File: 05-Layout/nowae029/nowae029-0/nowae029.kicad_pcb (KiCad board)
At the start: 2 copper layers, 100 x 99.9 mm, 1 part

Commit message: WiP on microcontroller
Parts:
- added U1: STM32L073CBT6, LQFP:LQFP48_7x7_0.5, F.Cu at (100.0, 108.0)

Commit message: WiP: PCB components placing
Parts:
- added C201: 100n, CAPACITOR:CAPACITOR-0603, F.Cu at (108.6, 107.0)
- added C202: 15p, CAPACITOR:CAPACITOR-0603, F.Cu at (238.7, 79.1)
- added C203: 15p, CAPACITOR:CAPACITOR-0603, F.Cu at (242.0, 79.1)
- added C204: 10u, CAPACITOR:CAPACITOR-1206, F.Cu at (107.2, 108.6)
- added C205: 100n, CAPACITOR:CAPACITOR-0603, F.Cu at (251.8, 72.2)
- added C206: 10u, CAPACITOR:CAPACITOR-1206, F.Cu at (236.6, 72.7)
- added C207: 10u, CAPACITOR:CAPACITOR-1206, F.Cu at (242.0, 69.2)
- added C208: 100n, CAPACITOR:CAPACITOR-0603, F.Cu at (245.2, 79.1)
- added C209: 10u, CAPACITOR:CAPACITOR-1206, F.Cu at (236.6, 76.1)
- added C210: 100n, CAPACITOR:CAPACITOR-0603, F.Cu at (251.8, 74.6)
- added C211: 100n, CAPACITOR:CAPACITOR-0603, F.Cu at (255.1, 72.2)
- added C301: 100n, CAPACITOR:CAPACITOR-0603, F.Cu at (165.1, 103.6)
- added C302: 100n, CAPACITOR:CAPACITOR-0603, F.Cu at (168.4, 103.6)
- added C303: 100n, CAPACITOR:CAPACITOR-0603, F.Cu at (171.6, 103.6)
- added C401: 1u, CAPACITOR:CAPACITOR-1206, F.Cu at (274.3, 69.2)
- added C402: 1u, CAPACITOR:CAPACITOR-1206, F.Cu at (268.8, 72.7)
- added C501: 4u7, CAPACITOR:CAPACITOR-1206, F.Cu at (91.6, 140.8)
- added C502: 100n, CAPACITOR:CAPACITOR-0603, F.Cu at (105.8, 145.0)
- added C503: 100n, CAPACITOR:CAPACITOR-0603, F.Cu at (114.6, 145.6)
- added C504: 100n, CAPACITOR:CAPACITOR-0603, F.Cu at (116.2, 145.6)
- added C601: 100n, CAPACITOR:CAPACITOR-0603, F.Cu at (165.1, 144.5)
- added C602: 100n, CAPACITOR:CAPACITOR-0603, F.Cu at (168.4, 144.5)
- added C603: 100n, CAPACITOR:CAPACITOR-0603, F.Cu at (171.6, 144.5)
- added D401: MBR0520, DIODE:DIODE-SOD123, F.Cu at (262.6, 72.1)
- added D402: MBR0520, DIODE:DIODE-SOD123, F.Cu at (262.6, 69.0)
- added D501: ESDA25P35, DIODE:DIODE-0805, F.Cu at (86.5, 141.0)
- added DL301: MISC, LEDs:LED-1206, F.Cu at (104.7, 76.1)
- added DL302: MISC, LEDs:LED-1206, B.Cu at (104.8, 76.0)
- added DL303: MISC, LEDs:LED-1206, F.Cu at (109.8, 79.0)
- added DL304: MISC, LEDs:LED-1206, F.Cu at (189.2, 69.2)
- added DL305: MISC, LEDs:LED-1206, F.Cu at (104.7, 91.1)
- added DL306: MISC, LEDs:LED-1206, F.Cu at (178.3, 83.2)
- added DL307: MISC, LEDs:LED-1206, F.Cu at (109.8, 94.0)
- added DL308: MISC, LEDs:LED-1206, F.Cu at (180.7, 79.8)
- added DL309: MISC, LEDs:LED-1206, F.Cu at (115.0, 97.0)
- added DL310: MISC, LEDs:LED-1206, F.Cu at (172.3, 90.3)
- added DL311: MISC, LEDs:LED-1206, F.Cu at (120.4, 100.0)
- added DL312: MISC, LEDs:LED-1206, F.Cu at (195.2, 69.2)
- added DL313: MISC, LEDs:LED-1206, F.Cu at (114.7, 111.7)
- added DL314: MISC, LEDs:LED-1206, F.Cu at (178.3, 86.7)
- added DL315: MISC, LEDs:LED-1206, F.Cu at (120.2, 114.6)
- added DL316: MISC, LEDs:LED-1206, F.Cu at (166.2, 100.7)
- added DL317: MISC, LEDs:LED-1206, F.Cu at (125.4, 117.6)
- added DL318: MISC, LEDs:LED-1206, F.Cu at (186.8, 79.6)
- added DL319: MISC, LEDs:LED-1206, F.Cu at (130.6, 120.6)
- added DL320: MISC, LEDs:LED-1206, F.Cu at (178.3, 90.1)
- added DL321: MISC, LEDs:LED-1206, F.Cu at (105.1, 121.1)
- added DL322: MISC, LEDs:LED-1206, F.Cu at (201.3, 69.2)
- added DL323: MISC, LEDs:LED-1206, F.Cu at (112.0, 124.8)
- added DL324: MISC, LEDs:LED-1206, F.Cu at (184.4, 86.7)
- added DL325: MISC, LEDs:LED-1206, F.Cu at (118.9, 128.9)
- added DL326: MISC, LEDs:LED-1206, F.Cu at (172.3, 100.7)
- added DL327: MISC, LEDs:LED-1206, F.Cu at (125.5, 132.5)
- added DL328: MISC, LEDs:LED-1206, F.Cu at (192.8, 79.6)
- added DL329: MISC, LEDs:LED-1206, F.Cu at (132.4, 136.4)
- added DL330: MISC, LEDs:LED-1206, F.Cu at (184.4, 90.1)
- added DL331: MISC, LEDs:LED-1206, F.Cu at (139.4, 140.4)
- added DL332: MISC, LEDs:LED-1206, F.Cu at (207.3, 69.2)
- added DL333: MISC, LEDs:LED-1206, F.Cu at (178.3, 97.0)
- added DL334: MISC, LEDs:LED-1206, F.Cu at (190.4, 86.5)
- added DL335: MISC, LEDs:LED-1206, F.Cu at (196.5, 83.0)
- added DL336: MISC, LEDs:LED-1206, F.Cu at (178.3, 100.5)
- added DL337: MISC, LEDs:LED-1206, F.Cu at (184.4, 93.6)
- added DL338: MISC, LEDs:LED-1206, F.Cu at (198.9, 79.6)
- added DL339: MISC, LEDs:LED-1206, F.Cu at (204.9, 76.1)
- added DL340: MISC, LEDs:LED-1206, F.Cu at (190.4, 89.9)
- added DL341: MISC, LEDs:LED-1206, F.Cu at (183.1, 69.2)
- added DL342: MISC, LEDs:LED-1206, F.Cu at (213.4, 69.2)
- added DL343: MISC, LEDs:LED-1206, F.Cu at (166.2, 83.4)
- added DL344: MISC, LEDs:LED-1206, F.Cu at (207.3, 72.7)
- added DL345: MISC, LEDs:LED-1206, F.Cu at (174.7, 76.3)
- added DL346: MISC, LEDs:LED-1206, F.Cu at (174.7, 79.8)
- added DL347: MISC, LEDs:LED-1206, F.Cu at (172.3, 83.4)
- added DL348: MISC, LEDs:LED-1206, F.Cu at (166.2, 86.9)
- added DL601: MISC, LEDs:LED-1206, F.Cu at (95.2, 76.0)
- added DL602: MISC, LEDs:LED-1206, F.Cu at (207.3, 113.6)
- added DL603: MISC, LEDs:LED-1206, F.Cu at (90.2, 79.0)
- added DL604: MISC, LEDs:LED-1206, F.Cu at (178.3, 141.4)
- added DL605: MISC, LEDs:LED-1206, F.Cu at (95.0, 91.2)
- added DL606: MISC, LEDs:LED-1206, F.Cu at (190.4, 127.4)
- added DL607: MISC, LEDs:LED-1206, F.Cu at (90.0, 94.0)
- added DL608: MISC, LEDs:LED-1206, F.Cu at (207.3, 110.1)
- added DL609: MISC, LEDs:LED-1206, F.Cu at (84.8, 97.0)
- added DL610: MISC, LEDs:LED-1206, F.Cu at (184.4, 131.0)
- added DL611: MISC, LEDs:LED-1206, F.Cu at (79.4, 100.0)
- added DL612: MISC, LEDs:LED-1206, F.Cu at (192.8, 120.5)
- added DL613: MISC, LEDs:LED-1206, F.Cu at (86.5, 110.9)
- added DL614: MISC, LEDs:LED-1206, F.Cu at (172.3, 141.6)
- added DL615: MISC, LEDs:LED-1206, F.Cu at (80.7, 114.1)
- added DL616: MISC, LEDs:LED-1206, F.Cu at (184.4, 127.6)
- added DL617: MISC, LEDs:LED-1206, F.Cu at (75.0, 117.2)
- added DL618: MISC, LEDs:LED-1206, F.Cu at (201.3, 110.1)
- added DL619: MISC, LEDs:LED-1206, F.Cu at (69.4, 120.4)
- added DL620: MISC, LEDs:LED-1206, F.Cu at (178.3, 131.0)
- added DL621: MISC, LEDs:LED-1206, F.Cu at (94.6, 121.2)
- added DL622: MISC, LEDs:LED-1206, F.Cu at (186.8, 120.5)
- added DL623: MISC, LEDs:LED-1206, F.Cu at (88.2, 124.8)
- added DL624: MISC, LEDs:LED-1206, F.Cu at (166.2, 141.6)
- added DL625: MISC, LEDs:LED-1206, F.Cu at (81.0, 128.8)
- added DL626: MISC, LEDs:LED-1206, F.Cu at (178.3, 127.6)
- added DL627: MISC, LEDs:LED-1206, F.Cu at (74.6, 132.4)
- added DL628: MISC, LEDs:LED-1206, F.Cu at (195.2, 110.1)
- added DL629: MISC, LEDs:LED-1206, F.Cu at (67.6, 136.4)
- added DL630: MISC, LEDs:LED-1206, F.Cu at (172.3, 131.2)
- added DL631: MISC, LEDs:LED-1206, F.Cu at (60.4, 140.4)
- added DL632: MISC, LEDs:LED-1206, F.Cu at (180.7, 120.7)
- added DL633: MISC, LEDs:LED-1206, F.Cu at (166.2, 134.7)
- added DL634: MISC, LEDs:LED-1206, F.Cu at (178.3, 124.1)
- added DL635: MISC, LEDs:LED-1206, F.Cu at (172.3, 127.8)
- added DL636: MISC, LEDs:LED-1206, F.Cu at (189.2, 110.1)
- added DL637: MISC, LEDs:LED-1206, F.Cu at (183.1, 113.6)
- added DL638: MISC, LEDs:LED-1206, F.Cu at (166.2, 131.2)
- added DL639: MISC, LEDs:LED-1206, F.Cu at (180.7, 117.2)
- added DL640: MISC, LEDs:LED-1206, F.Cu at (174.7, 120.7)
- added DL641: MISC, LEDs:LED-1206, F.Cu at (172.3, 124.3)
- added DL642: MISC, LEDs:LED-1206, F.Cu at (166.2, 127.8)
- added DL643: MISC, LEDs:LED-1206, F.Cu at (183.1, 110.1)
- added DL644: MISC, LEDs:LED-1206, F.Cu at (174.7, 117.2)
- added DL645: MISC, LEDs:LED-1206, F.Cu at (166.2, 124.3)
- added DL646: MISC, LEDs:LED-1206, F.Cu at (204.9, 117.0)
- added DL647: MISC, LEDs:LED-1206, F.Cu at (198.9, 120.5)
- added DL648: MISC, LEDs:LED-1206, F.Cu at (213.4, 110.1)
- added P501: 632722110112, CONNECTOR:USB3.1-C_WE-632722110112, F.Cu at (89.6, 145.2)
- added R201: 4k7, RESISTOR:RESISTOR-1206, F.Cu at (247.5, 76.1)
- added R202: 4k7, RESISTOR:RESISTOR-1206, F.Cu at (252.9, 69.2)
- added R203: 4k7, RESISTOR:RESISTOR-1206, F.Cu at (247.5, 72.7)
- added R204: 4k7, RESISTOR:RESISTOR-1206, F.Cu at (242.0, 76.1)
- added R205: 0, RESISTOR:RESISTOR-1206, F.Cu at (247.5, 69.2)
- added R206: 10k, RESISTOR:RESISTOR-1206, F.Cu at (242.0, 72.7)
- added R301: 270, RESISTOR:RESISTOR-1206, F.Cu at (202.5, 83.0)
- added R302: 270, RESISTOR:RESISTOR-1206, F.Cu at (184.4, 97.0)
- added R303: 270, RESISTOR:RESISTOR-1206, F.Cu at (211.0, 76.1)
- added R304: 270, RESISTOR:RESISTOR-1206, F.Cu at (196.5, 89.9)
- added R305: 270, RESISTOR:RESISTOR-1206, F.Cu at (196.5, 86.5)
- added R306: 270, RESISTOR:RESISTOR-1206, F.Cu at (189.8, 97.0)
- added R307: 270, RESISTOR:RESISTOR-1206, F.Cu at (213.4, 72.7)
- added R308: 270, RESISTOR:RESISTOR-1206, F.Cu at (184.4, 100.5)
- added R309: 270, RESISTOR:RESISTOR-1206, F.Cu at (190.4, 93.4)
- added R310: 270, RESISTOR:RESISTOR-1206, F.Cu at (204.9, 79.6)
- added R311: 270, RESISTOR:RESISTOR-1206, F.Cu at (217.7, 93.4)
- added R312: 270, RESISTOR:RESISTOR-1206, F.Cu at (211.6, 100.3)
- added R313: 270, RESISTOR:RESISTOR-1206, F.Cu at (223.7, 86.5)
- added R314: 270, RESISTOR:RESISTOR-1206, F.Cu at (211.6, 96.8)
- added R315: 270, RESISTOR:RESISTOR-1206, F.Cu at (218.3, 89.9)
- added R316: 270, RESISTOR:RESISTOR-1206, F.Cu at (226.7, 79.6)
- added R317: 270, RESISTOR:RESISTOR-1206, F.Cu at (212.2, 93.4)
- added R318: 270, RESISTOR:RESISTOR-1206, F.Cu at (206.2, 100.3)
- added R319: 270, RESISTOR:RESISTOR-1206, F.Cu at (224.3, 83.0)
- added R320: 270, RESISTOR:RESISTOR-1206, F.Cu at (218.3, 86.5)
- added R321: 270, RESISTOR:RESISTOR-1206, F.Cu at (206.2, 96.8)
- added R322: 270, RESISTOR:RESISTOR-1206, F.Cu at (212.8, 89.9)
- added R323: 270, RESISTOR:RESISTOR-1206, F.Cu at (227.3, 76.1)
- added R324: 270, RESISTOR:RESISTOR-1206, F.Cu at (221.3, 79.6)
- added R325: 270, RESISTOR:RESISTOR-1206, F.Cu at (206.8, 93.4)
- added R326: 270, RESISTOR:RESISTOR-1206, F.Cu at (200.7, 100.3)
- added R327: 270, RESISTOR:RESISTOR-1206, F.Cu at (218.9, 83.0)
- added R328: 270, RESISTOR:RESISTOR-1206, F.Cu at (212.8, 86.5)
- added R329: 270, RESISTOR:RESISTOR-1206, F.Cu at (200.7, 96.8)
- added R330: 270, RESISTOR:RESISTOR-1206, F.Cu at (224.3, 72.7)
- added R331: 270, RESISTOR:RESISTOR-1206, F.Cu at (207.4, 89.9)
- added R332: 270, RESISTOR:RESISTOR-1206, F.Cu at (221.9, 76.1)
- added R333: 270, RESISTOR:RESISTOR-1206, F.Cu at (215.8, 79.6)
- added R334: 270, RESISTOR:RESISTOR-1206, F.Cu at (201.3, 93.4)
- added R335: 270, RESISTOR:RESISTOR-1206, F.Cu at (195.3, 100.3)
- added R336: 270, RESISTOR:RESISTOR-1206, F.Cu at (213.4, 83.0)
- added R337: 270, RESISTOR:RESISTOR-1206, F.Cu at (207.4, 86.5)
- added R338: 270, RESISTOR:RESISTOR-1206, F.Cu at (224.9, 69.2)
- added R339: 270, RESISTOR:RESISTOR-1206, F.Cu at (195.3, 96.8)
- added R340: 270, RESISTOR:RESISTOR-1206, F.Cu at (218.8, 72.7)
- added R341: 270, RESISTOR:RESISTOR-1206, F.Cu at (201.9, 89.9)
- added R342: 270, RESISTOR:RESISTOR-1206, F.Cu at (216.4, 76.1)
- added R343: 270, RESISTOR:RESISTOR-1206, F.Cu at (210.4, 79.6)
- added R344: 270, RESISTOR:RESISTOR-1206, F.Cu at (195.9, 93.4)
- added R345: 270, RESISTOR:RESISTOR-1206, F.Cu at (189.8, 100.5)
- added R346: 270, RESISTOR:RESISTOR-1206, F.Cu at (208.0, 83.0)
- added R347: 270, RESISTOR:RESISTOR-1206, F.Cu at (201.9, 86.5)
- added R348: 270, RESISTOR:RESISTOR-1206, F.Cu at (219.4, 69.2)
- added R401: 100k, RESISTOR:RESISTOR-1206, F.Cu at (268.8, 69.2)
- added R402: 100k, RESISTOR:RESISTOR-1206, F.Cu at (262.5, 75.3)
- added R601: 270, RESISTOR:RESISTOR-1206, F.Cu at (95.4, 79.2)
- added R602: 270, RESISTOR:RESISTOR-1206, F.Cu at (217.7, 134.3)
- added R603: 270, RESISTOR:RESISTOR-1206, F.Cu at (91.2, 81.6)
- added R604: 270, RESISTOR:RESISTOR-1206, F.Cu at (218.3, 130.8)
- added R605: 270, RESISTOR:RESISTOR-1206, F.Cu at (184.4, 137.9)
- added R606: 270, RESISTOR:RESISTOR-1206, F.Cu at (223.7, 127.4)
- added R607: 270, RESISTOR:RESISTOR-1206, F.Cu at (196.5, 127.4)
- added R608: 270, RESISTOR:RESISTOR-1206, F.Cu at (202.5, 123.9)
- added R609: 270, RESISTOR:RESISTOR-1206, F.Cu at (184.4, 141.4)
- added R610: 270, RESISTOR:RESISTOR-1206, F.Cu at (190.4, 134.3)
- added R611: 270, RESISTOR:RESISTOR-1206, F.Cu at (204.9, 120.5)
- added R612: 270, RESISTOR:RESISTOR-1206, F.Cu at (211.0, 117.0)
- added R613: 270, RESISTOR:RESISTOR-1206, F.Cu at (196.5, 130.8)
- added R614: 270, RESISTOR:RESISTOR-1206, F.Cu at (189.8, 137.9)
- added R615: 270, RESISTOR:RESISTOR-1206, F.Cu at (213.4, 113.6)
- added R616: 270, RESISTOR:RESISTOR-1206, F.Cu at (219.4, 110.1)
- added R617: 270, RESISTOR:RESISTOR-1206, F.Cu at (201.9, 127.4)
- added R618: 270, RESISTOR:RESISTOR-1206, F.Cu at (208.0, 123.9)
- added R619: 270, RESISTOR:RESISTOR-1206, F.Cu at (189.8, 141.4)
- added R620: 270, RESISTOR:RESISTOR-1206, F.Cu at (195.9, 134.3)
- added R621: 270, RESISTOR:RESISTOR-1206, F.Cu at (210.4, 120.5)
- added R622: 270, RESISTOR:RESISTOR-1206, F.Cu at (216.4, 117.0)
- added R623: 270, RESISTOR:RESISTOR-1206, F.Cu at (201.9, 130.8)
- added R624: 270, RESISTOR:RESISTOR-1206, F.Cu at (218.8, 113.6)
- added R625: 270, RESISTOR:RESISTOR-1206, F.Cu at (195.3, 137.7)
- added R626: 270, RESISTOR:RESISTOR-1206, F.Cu at (224.9, 110.1)
- added R627: 270, RESISTOR:RESISTOR-1206, F.Cu at (207.4, 127.4)
- added R628: 270, RESISTOR:RESISTOR-1206, F.Cu at (213.4, 123.9)
- added R629: 270, RESISTOR:RESISTOR-1206, F.Cu at (195.3, 141.2)
- added R630: 270, RESISTOR:RESISTOR-1206, F.Cu at (201.3, 134.3)
- added R631: 270, RESISTOR:RESISTOR-1206, F.Cu at (215.8, 120.5)
- added R632: 270, RESISTOR:RESISTOR-1206, F.Cu at (221.9, 117.0)
- added R633: 270, RESISTOR:RESISTOR-1206, F.Cu at (207.4, 130.8)
- added R634: 270, RESISTOR:RESISTOR-1206, F.Cu at (224.3, 113.6)
- added R635: 270, RESISTOR:RESISTOR-1206, F.Cu at (200.7, 137.7)
- added R636: 270, RESISTOR:RESISTOR-1206, F.Cu at (212.8, 127.4)
- added R637: 270, RESISTOR:RESISTOR-1206, F.Cu at (218.9, 123.9)
- added R638: 270, RESISTOR:RESISTOR-1206, F.Cu at (200.7, 141.2)
- added R639: 270, RESISTOR:RESISTOR-1206, F.Cu at (206.8, 134.3)
- added R640: 270, RESISTOR:RESISTOR-1206, F.Cu at (221.3, 120.5)
- added R641: 270, RESISTOR:RESISTOR-1206, F.Cu at (227.3, 117.0)
- added R642: 270, RESISTOR:RESISTOR-1206, F.Cu at (212.8, 130.8)
- added R643: 270, RESISTOR:RESISTOR-1206, F.Cu at (206.2, 137.7)
- added R644: 270, RESISTOR:RESISTOR-1206, F.Cu at (218.3, 127.4)
- added R645: 270, RESISTOR:RESISTOR-1206, F.Cu at (224.3, 123.9)
- added R646: 270, RESISTOR:RESISTOR-1206, F.Cu at (206.2, 141.2)
- added R647: 270, RESISTOR:RESISTOR-1206, F.Cu at (212.2, 134.3)
- added R648: 270, RESISTOR:RESISTOR-1206, F.Cu at (226.7, 120.5)
- added U301: TCA9554PWR, SOP:TSSOP16_4.4x5.0_0.65, F.Cu at (110.2, 137.2)
- added U302: TCA9554PWR, SOP:TSSOP16_4.4x5.0_0.65, F.Cu at (124.4, 143.6)
- added U303: TCA9554PWR, SOP:TSSOP16_4.4x5.0_0.65, F.Cu at (176.2, 71.2)
- added U401: TLV70233DBV, SOT:SOT23-5, F.Cu at (273.9, 73.1)
- added U501: FT230XS, SOP:SSOP16_3.9x4.9_0.635, F.Cu at (110.2, 145.2)
- added U601: TCA9554PWR, SOP:TSSOP16_4.4x5.0_0.65, F.Cu at (89.6, 133.8)
- added U602: TCA9554PWR, SOP:TSSOP16_4.4x5.0_0.65, F.Cu at (76.0, 143.6)
- added U603: TCA9554PWR, SOP:TSSOP16_4.4x5.0_0.65, F.Cu at (167.7, 112.1)
- moved G*** 58.3 mm to (180.0, 153.0)
- moved U1 4.03 mm to (100.0, 104.0)
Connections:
- net Net-(U1-Pad15) renamed /Microcontroller/STAR
- net Net-(U1-Pad34) renamed /Microcontroller/SWDIO
- net Net-(U1-Pad37) renamed /Microcontroller/SWCLK
- U1 pad 10: Net-(U1-Pad10) -> /Power Supply/BATTERY_STATUS
- U1 pad 21: Net-(U1-Pad21) -> /B_EXT_SDA
- U1 pad 22: Net-(U1-Pad22) -> /B_EXT_SCL
- U1 pad 23: Net-(U1-Pad23) -> GND
- U1 pad 24: Net-(U1-Pad24) -> /Microcontroller/VDD_MCU
- U1 pad 30: Net-(U1-Pad30) -> /Communication/COMM_RX
- U1 pad 31: Net-(U1-Pad31) -> /Communication/COMM_TX
- U1 pad 35: Net-(U1-Pad35) -> GND
- U1 pad 36: Net-(U1-Pad36) -> /Microcontroller/VDD_MCU
- U1 pad 42: Net-(U1-Pad42) -> /Branch1/BRANCH1_SCL
- U1 pad 43: Net-(U1-Pad43) -> /Branch1/BRANCH1_SDA
- U1 pad 47: Net-(U1-Pad47) -> GND
- U1 pad 48: Net-(U1-Pad48) -> /Microcontroller/VDD_MCU
- U1 pad 7: Net-(U1-Pad7) -> /Microcontroller/RESET
- U1 pad 8: Net-(U1-Pad8) -> GND
- U1 pad 9: Net-(U1-Pad9) -> /Microcontroller/VDD_MCU

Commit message: WiP: components placing
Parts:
- removed U1: STM32L073CBT6, LQFP:LQFP48_7x7_0.5
- added U201: STM32L073CBT6, LQFP:LQFP48_7x7_0.5, F.Cu at (100.0, 105.3)
- DL602, DL604, DL606, DL608, DL610, DL612, DL614, DL616, DL618, DL620, DL622, DL624, DL626, DL628, DL630, DL632, R602, R604, R606, R608, R610, R612, R614, R616, R618, R620, R622, R624, R626, R628, R630, R632: moved to B.Cu
- moved R201 173.7 mm to (92.0, 153.6), turned to 270 degrees
- moved R203 173.0 mm to (94.6, 153.6), turned to 270 degrees
- moved C205 164.5 mm to (91.3, 108.1)
- moved R632 162.4 mm to (61.6, 143.2), turned to 30 degrees
- moved R205 159.5 mm to (94.4, 114.1), turned to 90 degrees
- moved R631 155.9 mm to (61.6, 143.2), turned to 30 degrees
- moved C210 154.2 mm to (102.4, 112.9), turned to 90 degrees
- moved C206 149.0 mm to (91.4, 106.1)
- moved C208 148.5 mm to (97.9, 98.0), turned to 270 degrees
- moved C207 144.7 mm to (100.0, 97.1), turned to 270 degrees
- moved R626 144.4 mm to (82.1, 131.7), turned to 30 degrees
- moved R628 137.9 mm to (76.0, 135.1), turned to 30 degrees
- moved R616 137.5 mm to (82.1, 116.7), turned to 30 degrees
- moved C209 137.4 mm to (104.5, 114.0), turned to 90 degrees
- moved R604 136.3 mm to (91.2, 81.6), turned to 30 degrees
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
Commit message: WiP: components placing
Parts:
- removed C303, C603: 100n, CAPACITOR:CAPACITOR-0603
- removed DL333, DL334, DL335, DL336, DL337, DL338, DL339, DL340, DL341, DL342, DL343, DL344, DL345, DL346, DL347, DL348, DL633, DL634, DL635, DL636, DL637, DL638, DL639, DL640, DL641, DL642, DL643, DL644, DL645, DL646, DL647, DL648: MISC, LEDs:LED-1206
- removed G***: LOGO, LOGO:LOGO_NOWAE_35MM_FSILK
- removed R333, R334, R335, R336, R337, R338, R339, R340, R341, R342, R343, R344, R345, R346, R347, R348, R633, R634, R635, R636, R637, R638, R639, R640, R641, R642, R643, R644, R645, R646, R647, R648: 270, RESISTOR:RESISTOR-1206
- removed U303, U603: TCA9554PWR, SOP:TSSOP16_4.4x5.0_0.65
- DL304, DL306, DL308, DL310, DL312, DL314, DL316, DL318, DL320, DL322, DL324, DL326, DL328, DL330, DL332, R302, R304: moved to B.Cu
- moved DL322 109.3 mm to (105.1, 121.1), turned to 330 degrees
- moved R307 106.9 mm to (109.3, 96.9), turned to 150 degrees
- moved R303 102.1 mm to (109.0, 81.7), turned to 150 degrees
- moved R311 98.4 mm to (119.7, 102.7), turned to 150 degrees
- moved DL332 98.4 mm to (139.4, 140.4), turned to 330 degrees
- moved R301 97.8 mm to (104.8, 79.3), turned to 330 degrees
- moved R305 91.9 mm to (104.9, 94.4), turned to 330 degrees
- moved R304 87.9 mm to (109.0, 81.7), turned to 150 degrees
- moved DL328 85.6 mm to (125.5, 132.5), turned to 330 degrees
- moved DL324 81.8 mm to (112.0, 124.8), turned to 330 degrees
- moved R302 81.5 mm to (104.8, 79.3), turned to 330 degrees
- moved DL312 80.9 mm to (120.4, 99.9), turned to 330 degrees
- moved DL304 80.0 mm to (109.8, 79.0), turned to 330 degrees
- moved R309 76.0 mm to (114.7, 99.9), turned to 330 degrees
- moved DL306 74.0 mm to (104.7, 91.1), turned to 330 degrees
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
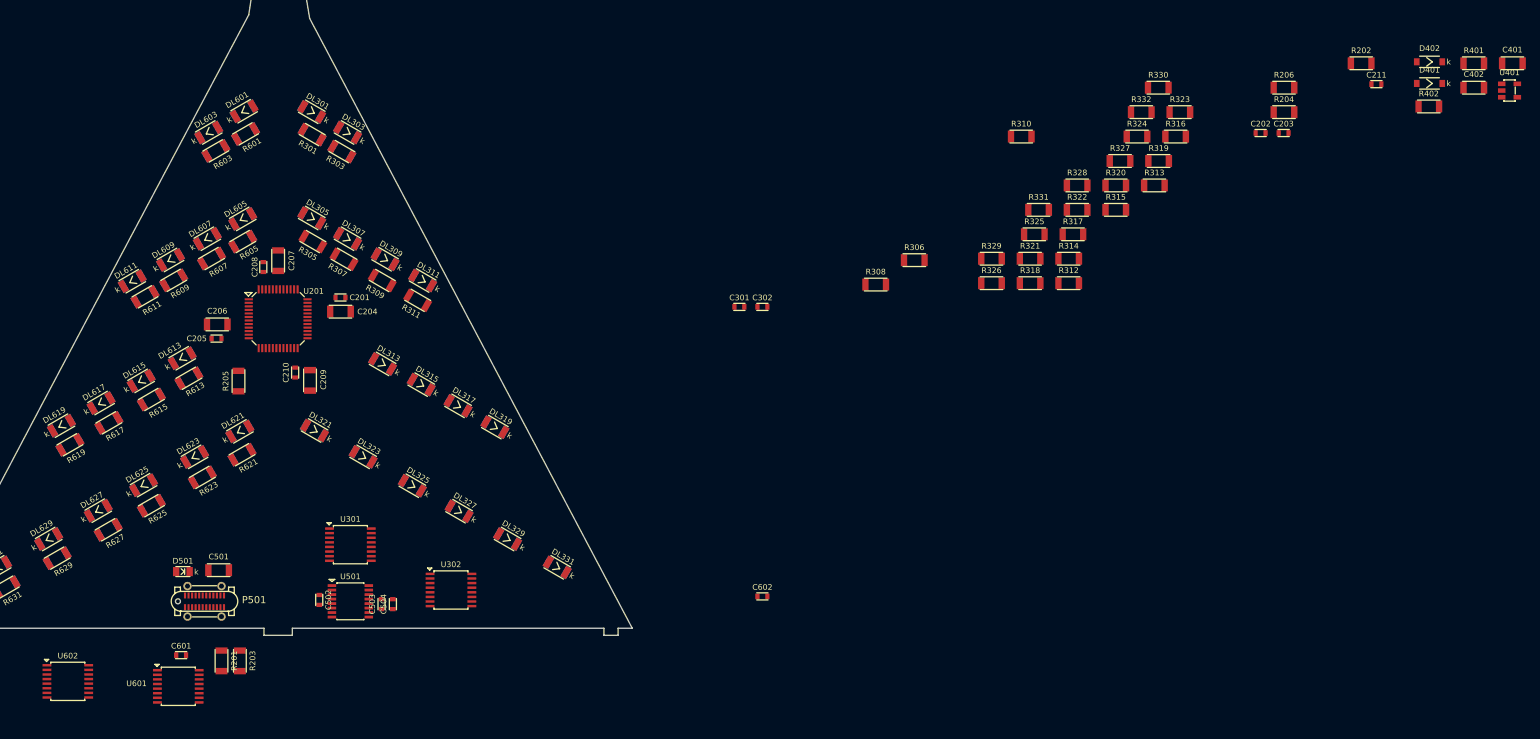
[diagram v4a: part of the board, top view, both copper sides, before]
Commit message: WiP: components placing Added some footprints
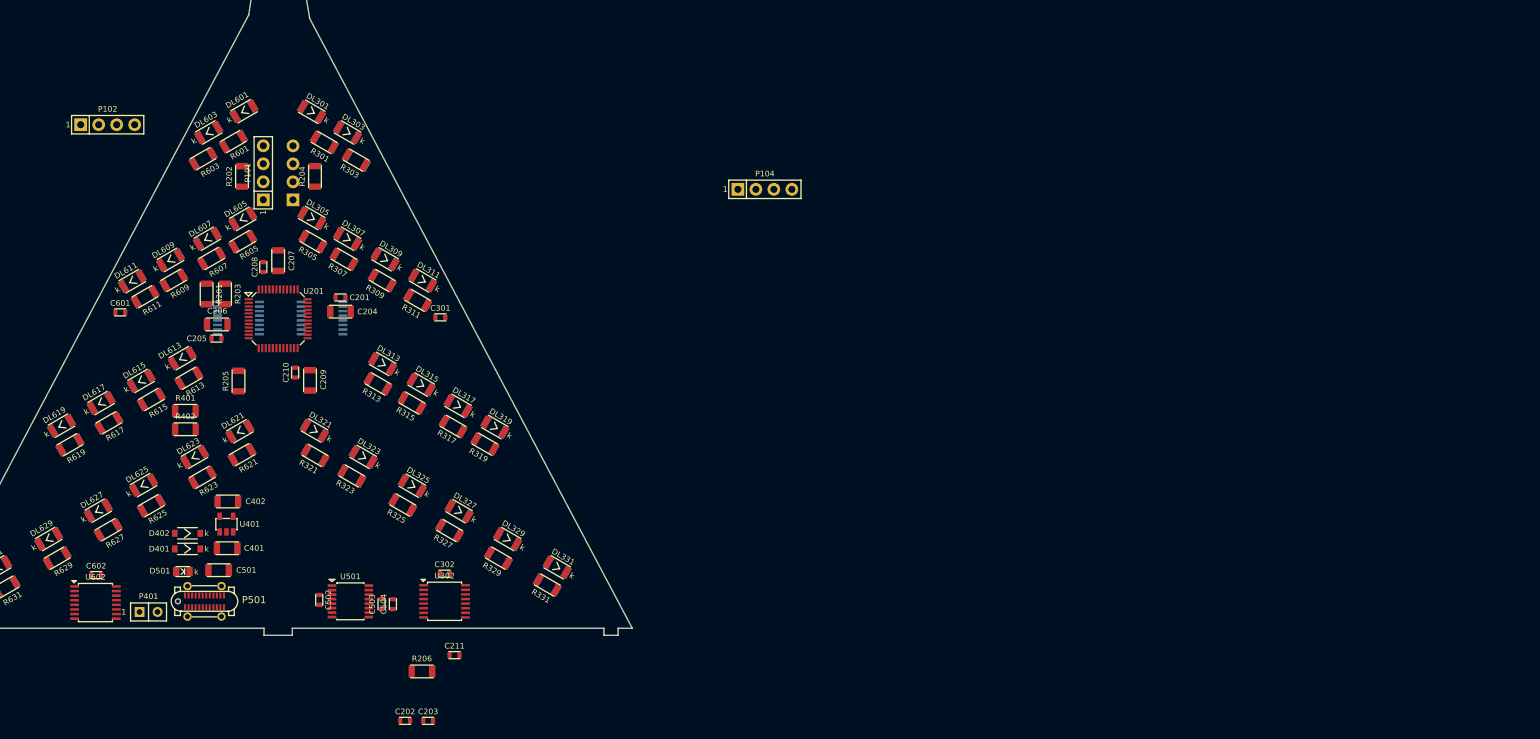
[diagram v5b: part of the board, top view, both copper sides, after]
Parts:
- added P101: COMM_3, CONNECTOR:CONN-STRIP-4x1-2.54, F.Cu at (97.9, 84.7)
- added P102: SUPPLY_3, CONNECTOR:CONN-STRIP-4x1-2.54, F.Cu at (75.9, 77.9)
- added P103: COMM_4, CONNECTOR:CONN-STRIP-4x1-2.54, B.Cu at (102.1, 84.7)
- added P104: SUPPLY_4, CONNECTOR:CONN-STRIP-4x1-2.54, F.Cu at (168.7, 87.0)
- added P401: BATTERY, CONNECTOR:CONN-STRIP-2x1-2.54, F.Cu at (81.7, 146.7)
- R306, R308, R310, R312, R314, R316, R318, R320, R322, R324, R326, R328, R330, R332, U301, U601: moved to B.Cu
- moved C401 194.0 mm to (92.8, 137.7)
- moved U401 191.2 mm to (92.7, 134.3), turned to 90 degrees
- moved R401 188.4 mm to (86.9, 118.3)
- moved D402 187.6 mm to (87.2, 135.6)
- moved D401 187.3 mm to (87.2, 137.8)
- moved C402 185.4 mm to (92.9, 131.1)
- moved R402 181.4 mm to (86.9, 120.9)
- moved R202 158.8 mm to (94.9, 85.2), turned to 90 degrees
- moved C211 153.1 mm to (124.9, 152.8)
- moved R206 147.0 mm to (120.3, 155.1)
- moved C202 146.6 mm to (117.9, 162.1)
- moved C203 146.6 mm to (121.2, 162.1)
- moved R204 137.1 mm to (105.2, 85.2), turned to 90 degrees
- moved R323 127.7 mm to (110.4, 127.5), turned to 150 degrees
- moved R324 120.8 mm to (110.4, 127.5), turned to 150 degrees
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
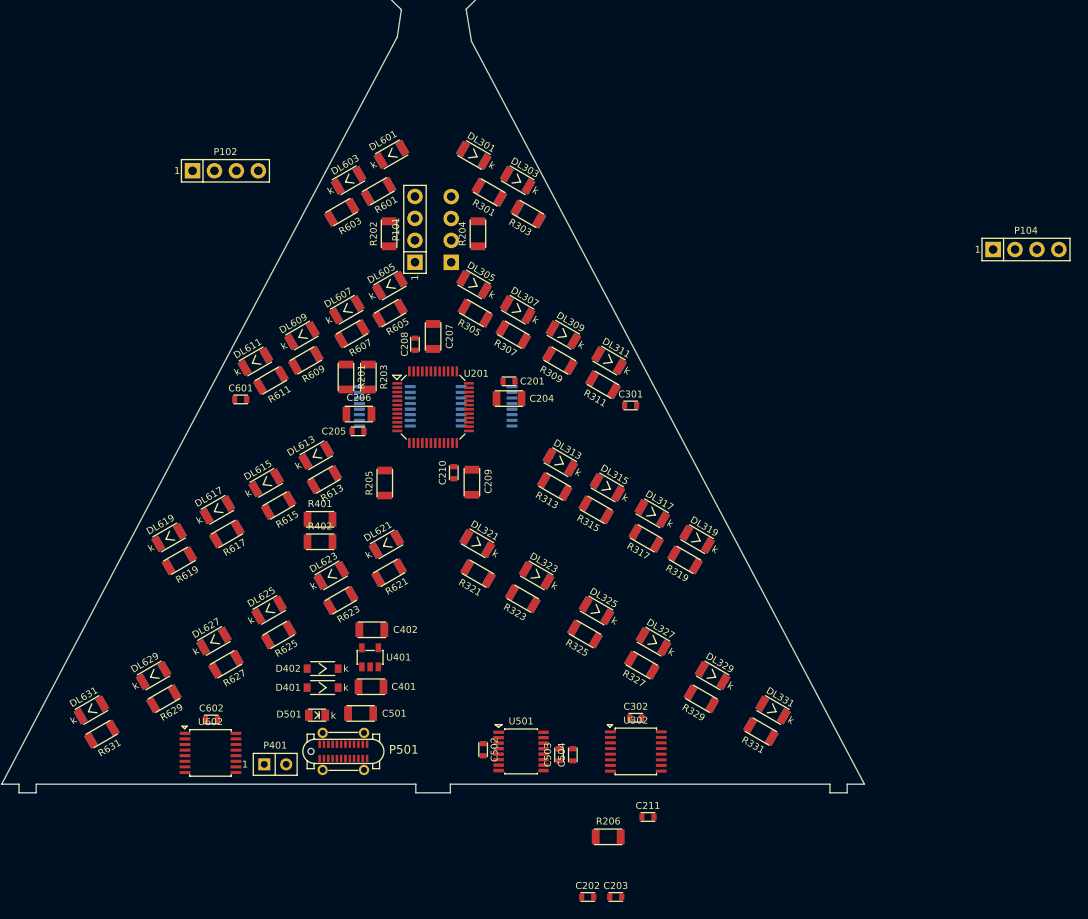
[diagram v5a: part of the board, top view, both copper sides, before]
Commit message: WiP: I don't like the LEDs position...
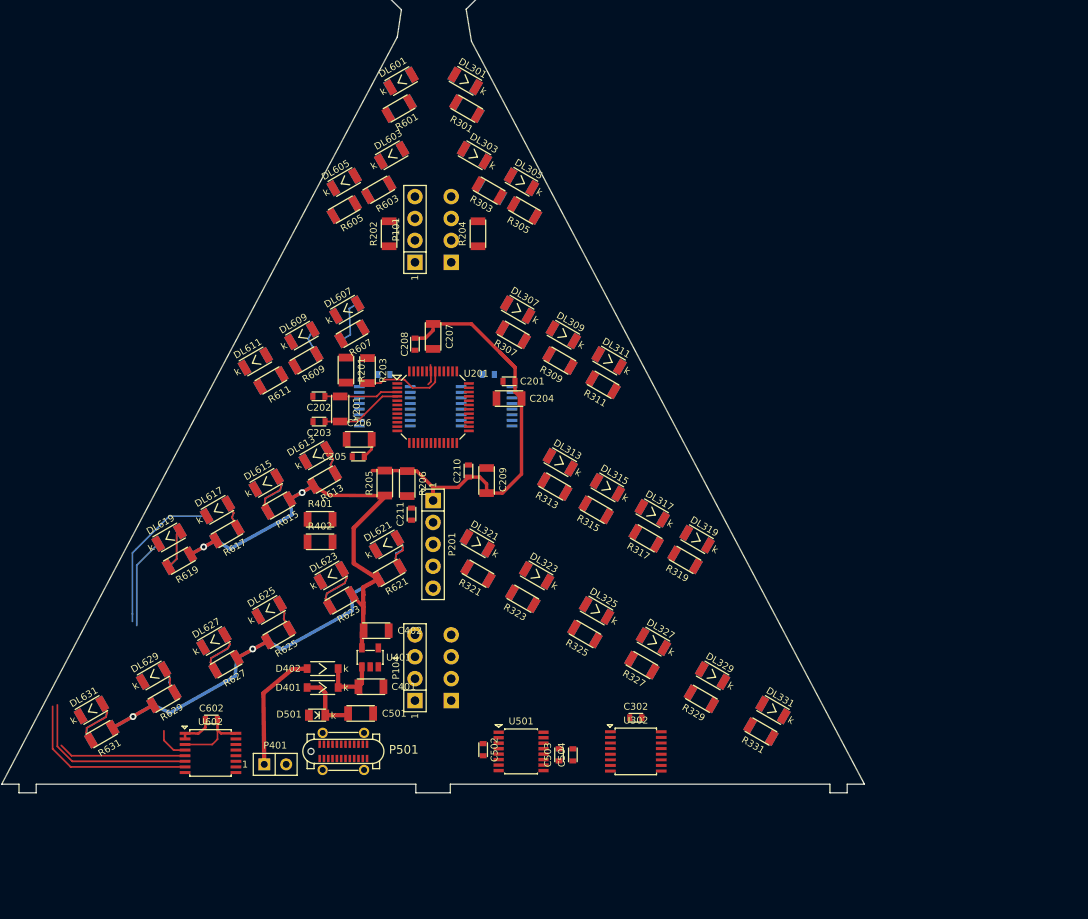
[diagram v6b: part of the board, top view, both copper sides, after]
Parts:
- added P201: DEBUG, CONNECTOR:CONN-STRIP-5x1-2.54, F.Cu at (100.0, 121.2)
- added Y201: 32768, CRYSTAL:CRYSTAL_1206, F.Cu at (89.2, 105.5)
- C301, C601, P102: moved to B.Cu
- moved P104 85.8 mm to (97.9, 135.5), turned to 90 degrees
- moved C202 65.9 mm to (86.8, 104.0), turned to 180 degrees
- moved C203 65.0 mm to (86.8, 107.0), turned to 180 degrees
- moved P102 63.3 mm to (102.1, 135.5), turned to 90 degrees
- moved R206 47.1 mm to (97.0, 114.2), turned to 270 degrees
- moved C211 44.5 mm to (97.5, 117.7), turned to 90 degrees
- moved C301 16.9 mm to (106.4, 101.5), turned to 180 degrees
- moved C601 16.9 mm to (94.3, 101.5), turned to 180 degrees
- moved R305 13.2 mm to (110.6, 82.5)
- moved R306 13.2 mm to (110.6, 82.5)
- moved DL605 13.1 mm to (89.7, 79.2)
- moved DL606 13.1 mm to (89.7, 79.2)
- moved R605 13.1 mm to (89.7, 82.4)
- moved R606 13.1 mm to (89.7, 82.4)
- moved DL305 13.1 mm to (110.2, 79.2)
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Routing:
- net +3.3V: track 0.00 -> 116.3 mm, vias 0 -> 4
- net /Microcontroller/VDD_MCU: track 0.00 -> 53.8 mm
- net /Branch2/B2_LINE10: track 0.00 -> 25.4 mm
- net /Branch2/B2_LINE9: track 0.00 -> 22.3 mm
- net /Branch2/B2_LINE12: track 0.00 -> 21.1 mm
- net /Branch2/B2_LINE11: track 0.00 -> 20.3 mm
- net Net-(D402-Pad1): track 0.00 -> 14.3 mm
- net /Branch1/BRANCH1_SCL: track 0.00 -> 9.93 mm
- net Net-(C203-Pad1): track 0.00 -> 9.58 mm
- net Net-(C202-Pad1): track 0.00 -> 8.61 mm
- net +VUSB: track 0.00 -> 7.68 mm
- net Net-(C401-Pad1): track 0.00 -> 7.06 mm
- net GND: track 0.00 -> 6.62 mm
- net Net-(DL631-Pad1): track 0.00 -> 5.91 mm
- net Net-(DL624-Pad1): track 0.00 -> 5.89 mm
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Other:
- net class Default: trace_width 0.25 -> 0.2
